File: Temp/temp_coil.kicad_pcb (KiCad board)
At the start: 2 copper layers, 0 parts

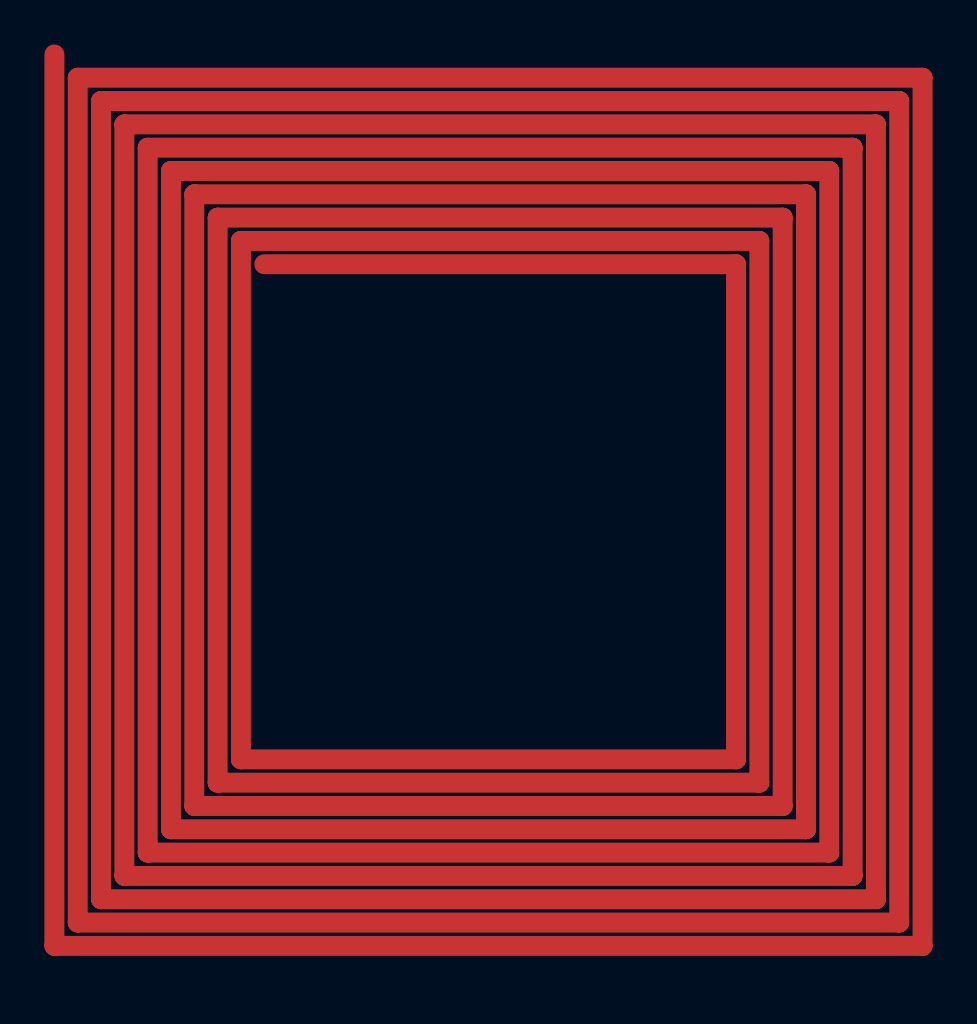
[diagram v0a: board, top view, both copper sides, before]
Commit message: Trace in correct position, but shapes not rendering properly
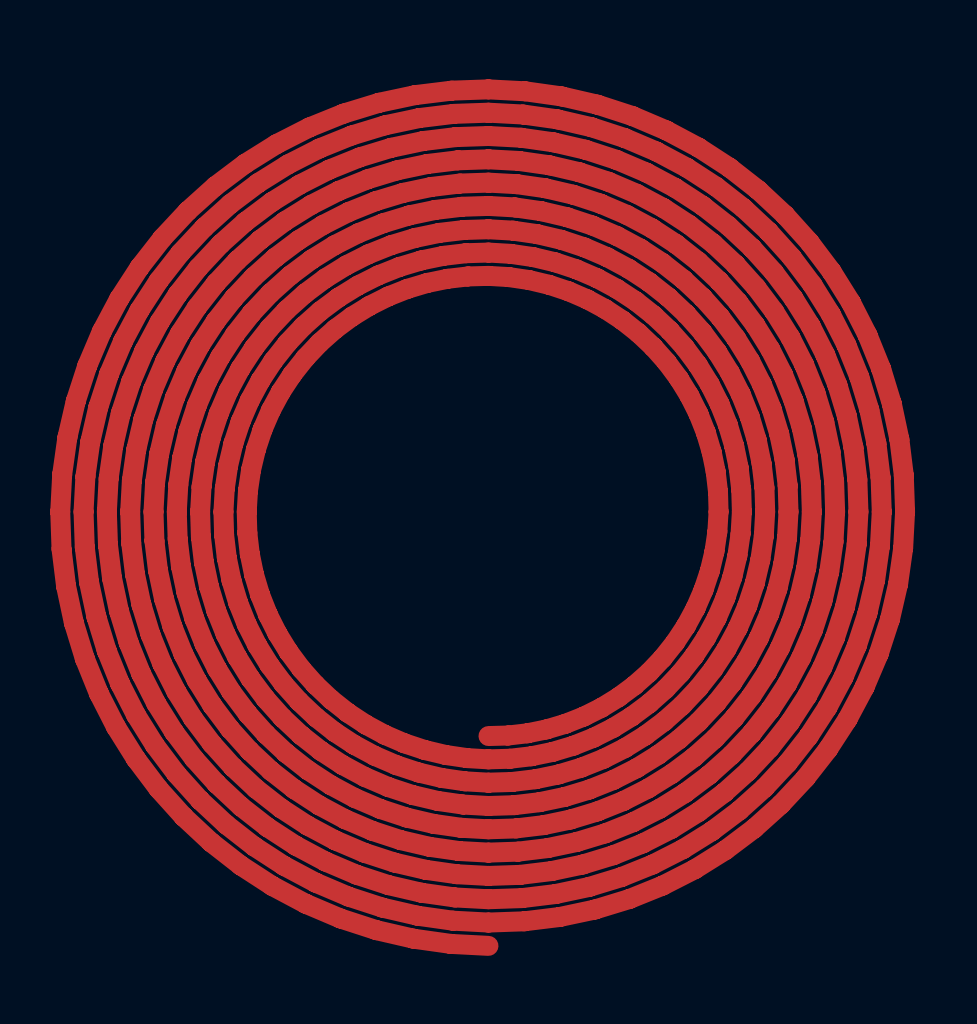
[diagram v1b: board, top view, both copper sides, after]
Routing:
- net (no net): track 1105.2 -> 838.1 mm

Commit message: Working pcbnew
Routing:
- net (no net): track 838.1 -> 1105.2 mm
